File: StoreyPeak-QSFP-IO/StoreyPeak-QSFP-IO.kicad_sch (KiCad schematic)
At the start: 28 parts, among them U1 QSFP_PCB-QSFP, U3 CH340G, X1 X322512MSB4SI

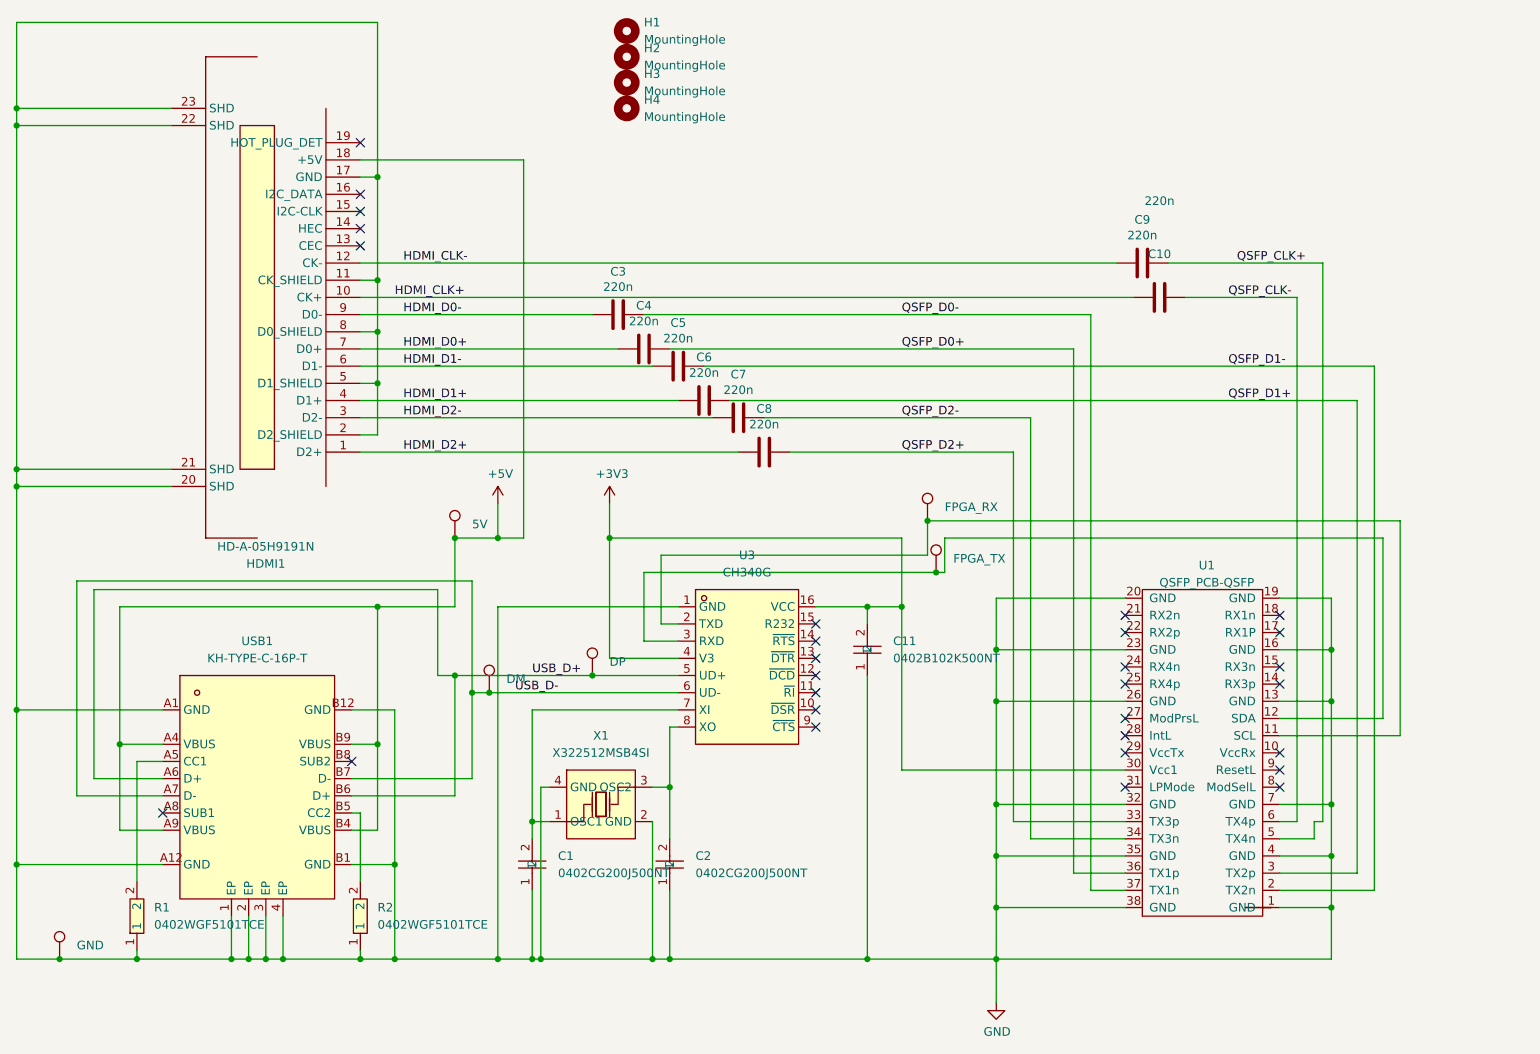
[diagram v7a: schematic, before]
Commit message: Change QSFP->HDMI mapping for better routing, skew match diffpairs
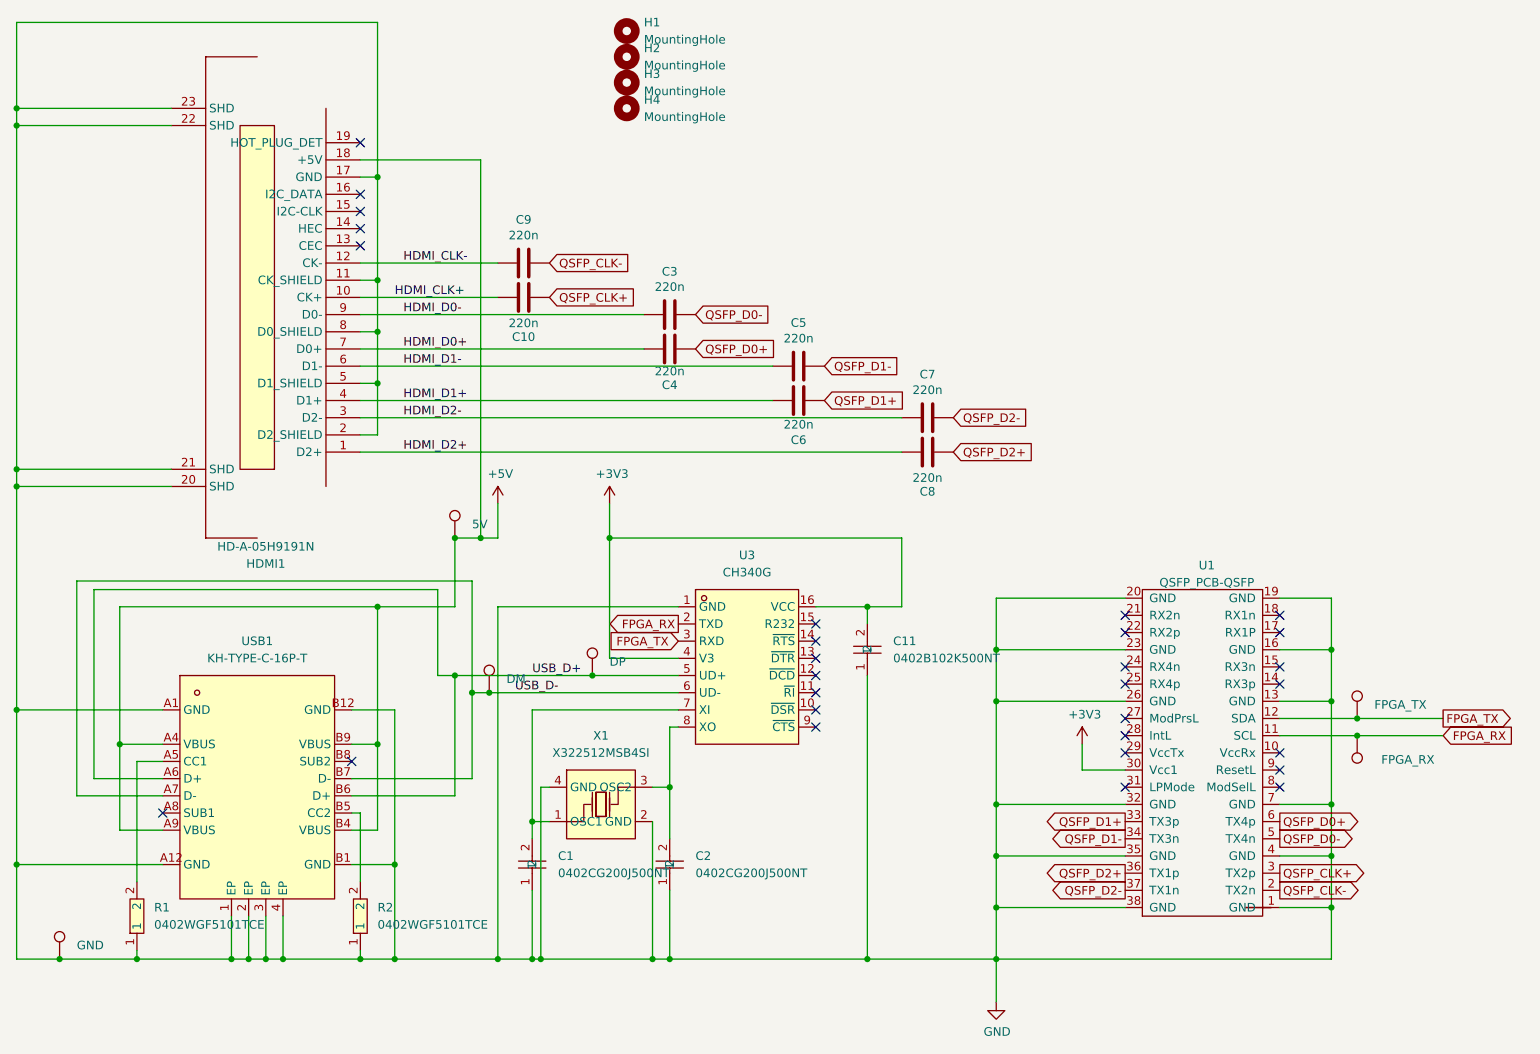
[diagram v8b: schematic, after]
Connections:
- net QSFP_CLK+: now also C10.1, U1.3 (TX2p); no longer C9.1, U1.5 (TX4n)
- net QSFP_CLK-: now also C9.1, U1.2 (TX2n); no longer C10.1, U1.6 (TX4p)
- net QSFP_D0+: now also U1.6 (TX4p); no longer U1.36 (TX1p)
- net QSFP_D0-: now also U1.5 (TX4n); no longer U1.37 (TX1n)
- net QSFP_D1+: now also U1.33 (TX3p); no longer U1.3 (TX2p)
- net QSFP_D1-: now also U1.34 (TX3n); no longer U1.2 (TX2n)
- net QSFP_D2+: now also U1.36 (TX1p); no longer U1.33 (TX3p)
- net QSFP_D2-: now also U1.37 (TX1n); no longer U1.34 (TX3n)
- net FPGA_RX: now reaches TP3.1, U1.11 (SCL), U3.2 (TXD)
- net FPGA_TX: now reaches TP4.1, U1.12 (SDA), U3.3 (RXD)
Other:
- moved on the sheet: C10, C3, C4, C5, C6, C7, C8, C9
